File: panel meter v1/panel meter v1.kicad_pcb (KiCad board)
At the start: 2 copper layers, 78.7 x 73.7 mm, 328 parts, among them J1 power switch, J10 REF_LO, J11 decimals, J12 lamp test, J13 display, J14 2, J15 3, J16 4, J17 1, J18 1776266-4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

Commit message: gerber zip
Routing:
- net /V-: track 49.0 -> 59.2 mm
- net GND: track 161.2 -> 169.9 mm

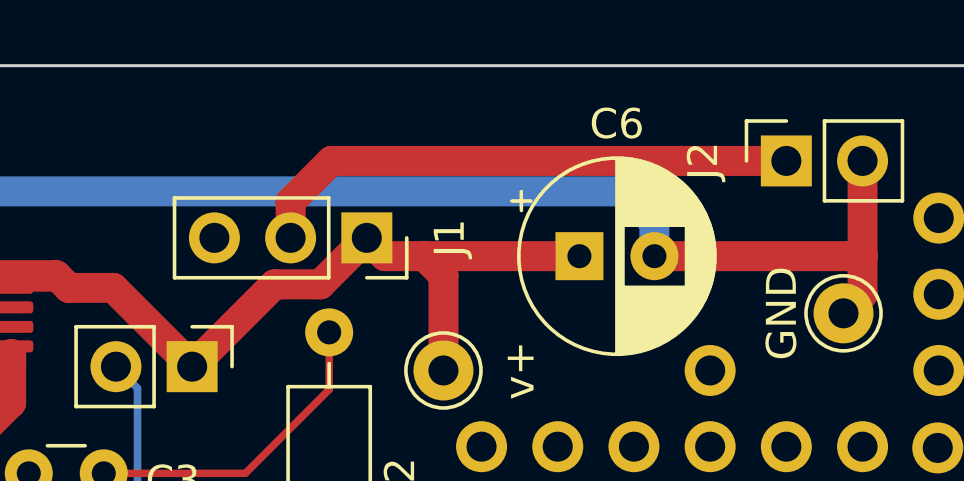
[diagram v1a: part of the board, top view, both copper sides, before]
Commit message: tweaked silk
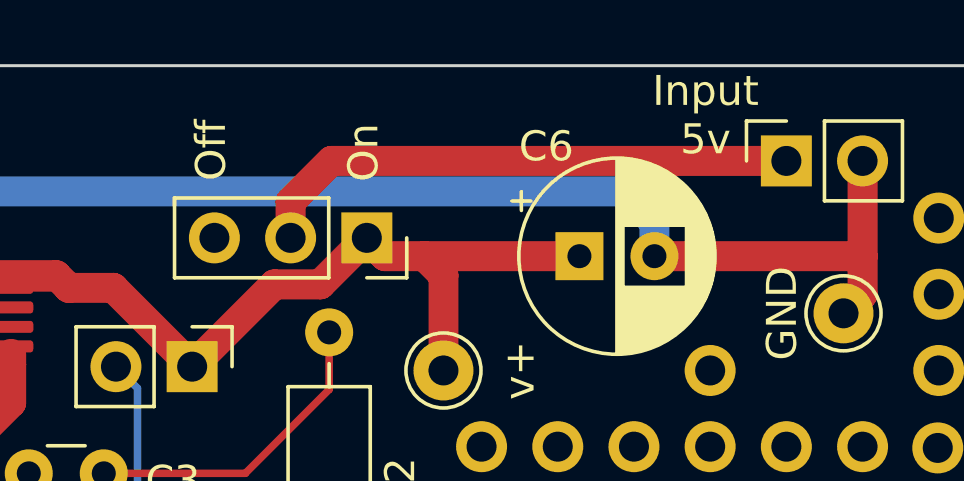
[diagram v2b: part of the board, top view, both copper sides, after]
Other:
- board text added: "Input 5v"
- board text added: "Off"
- board text added: "On"
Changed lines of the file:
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@@
     (property "Sheetname" "")
     (attr through_hole)
-    (fp_text reference "J1" (at 0 -2.77 90) (layer "F.SilkS")
+    (fp_text reference "J1" (at 0 -2.77 90) (layer "F.SilkS") hide
       (effects (font (size 1 1) (thickness 0.15)))
     )
@@
     (property "Sheetname" "")
     (attr through_hole)
-    (fp_text reference "J2" (at 0 -2.77 90) (layer "F.SilkS")
+    (fp_text reference "J2" (at 0.3302 5.0546 90) (layer "F.SilkS") hide
       (effects (font (size 1 1) (thickness 0.15)))
     )
@@
     (property "Sheetname" "")
     (attr through_hole)
-    (fp_text reference "C6" (at 1.25 -4.4) (layer "F.SilkS")
+    (fp_text reference "C6" (at -1.103621 -3.6576) (layer "F.SilkS")
       (effects (font (size 1 1) (thickness 0.15)))
     )
@@
     (effects (font (size 1 1) (thickness 0.15)))
   )
+  (gr_text "On" (at 95.123 43.5356 90) (layer "F.SilkS")
+    (effects (font (size 1 1) (thickness 0.15)))
+  )
   (gr_text "G1" (at 60.926471 63.424778 90) (layer "F.SilkS")
     (effects (font (size 1 1) (thickness 0.15)))
   )
+  (gr_text "Input\n5v" (at 106.5276 42.291) (layer "F.SilkS")
+    (effects (font (size 1 1) (thickness 0.15)))
+  )
   (gr_text "F1" (at 58.42 60.96 90) (layer "F.SilkS")
     (effects (font (size 1 1) (thickness 0.15)))
@@
     (effects (font (size 1 1) (thickness 0.15)))
   )
+  (gr_text "Off" (at 90.043 43.4594 90) (layer "F.SilkS")
+    (effects (font (size 1 1) (thickness 0.15)))
+  )
